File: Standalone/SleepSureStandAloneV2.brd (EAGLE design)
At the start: 62.3 x 37 mm, 66 parts, among them IC1 CP2104, Q1 mmbt2222, Q2 mmbt2222, Q3 DMG3415U, SW2 KMR2, U1 ADS1299-4PAG, U2 AP2112-3.3, U3 MCP73831T-2ACI/OT, X1 JSTPH, X2 ESP32_WROOM32_SKINNY, X4 20329

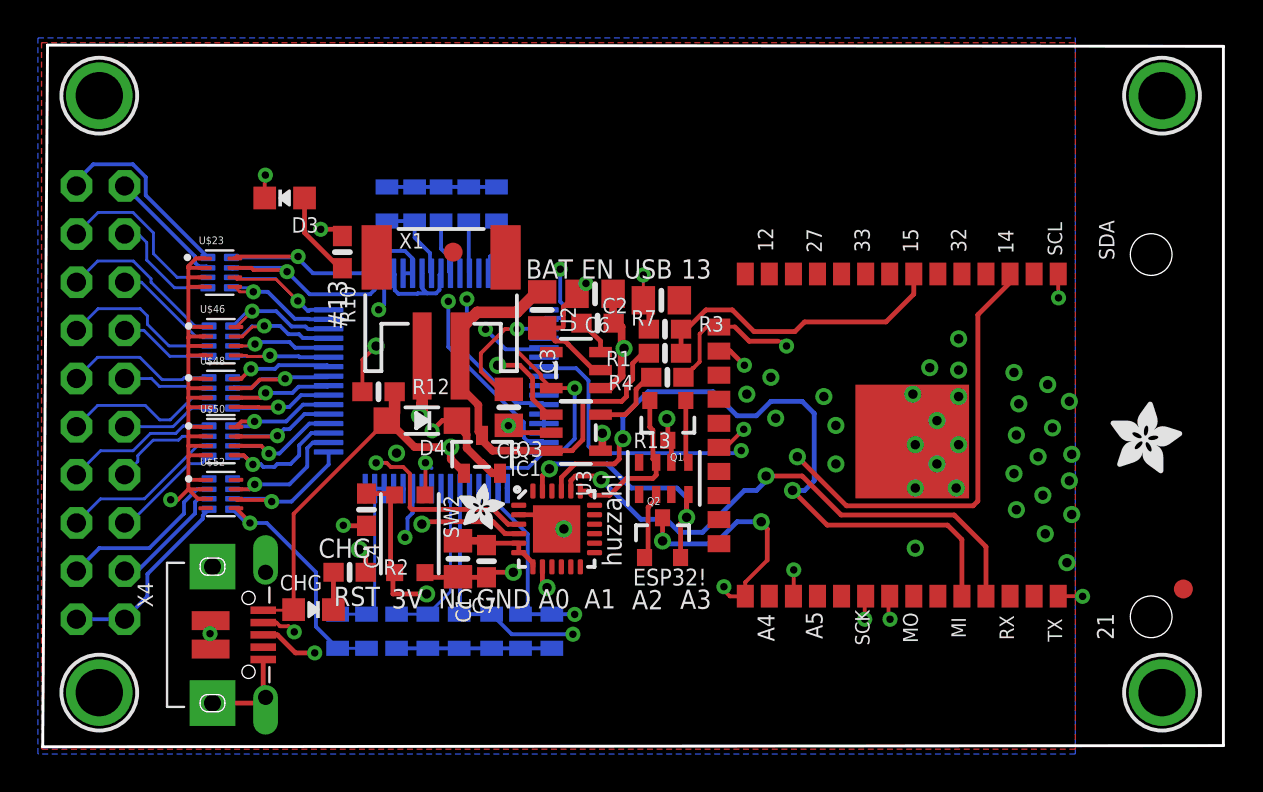
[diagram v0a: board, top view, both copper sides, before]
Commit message: modified design file and removed errors
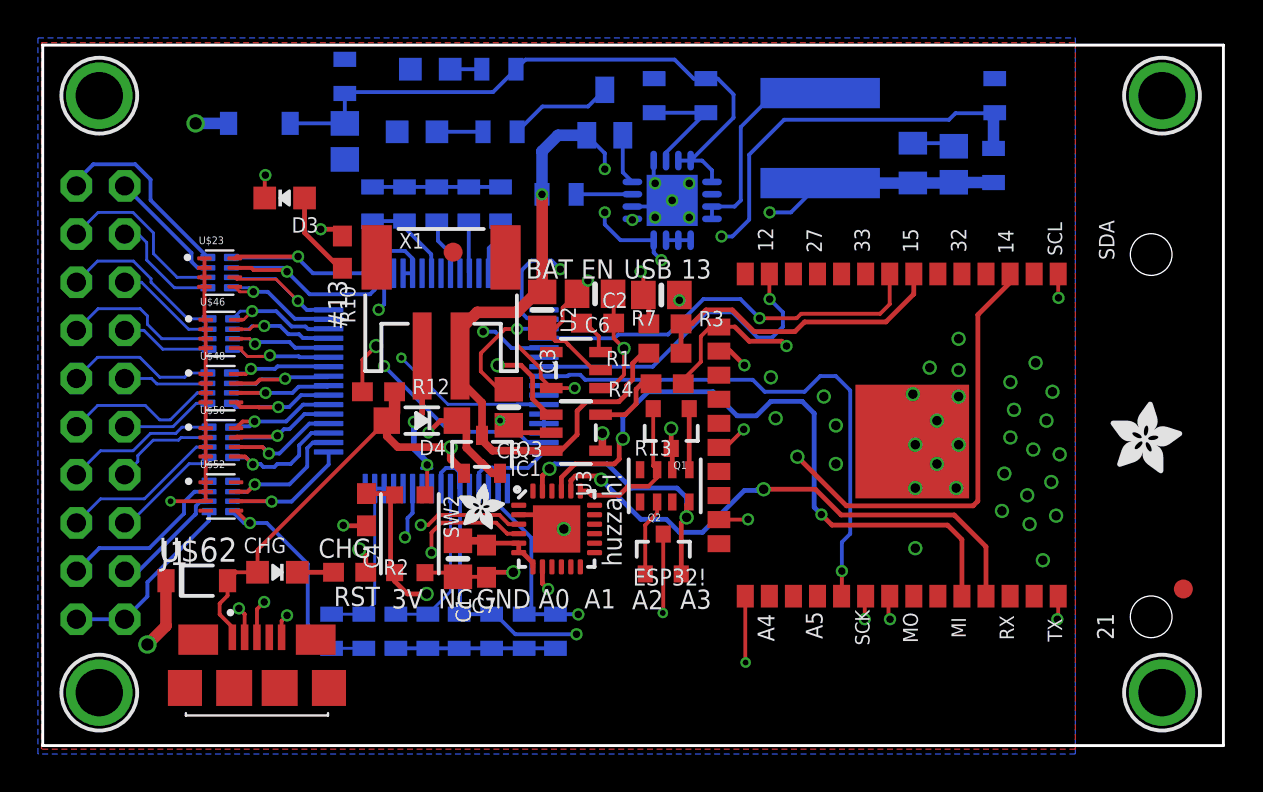
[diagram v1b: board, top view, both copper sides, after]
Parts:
- removed U$13: (no value), microbuilder:PCBFEAT-REV-040
- removed U$43: (no value), silks:HUZZAH32
- removed U$7: (no value), microbuilder:ADAFRUIT_5MM
- removed U$9: (no value), silks:FEATHERLOGO_MED
- removed X4: 20329, microbuilder:4UCONN_20329_V2
- added C17: 10uF, microbuilder:0805-NO
- added C18: 2.2uF, microbuilder:0805-NO
- added C19: 0.1uF, microbuilder:0805_10MGAP
- added C22: 100uF, SparkFun-Capacitors:0805
- added J1: 10118192-0002LF, ADS_Feather:AMPHENOL_10118192-0002LF
- added LED1: RED, microbuilder:CHIPLED_0805_NOOUTLINE
- added LED2: BLUE, microbuilder:CHIPLED_0805_NOOUTLINE
- added R11, R9: 1k, SparkFun-Resistors:0805
- added R16: 1.87M, SparkFun-Resistors:0805
- added R17: 340k, SparkFun-Resistors:0805
- added R18: 1.8M, SparkFun-Resistors:0805
- added R19, R5: 200k, SparkFun-Resistors:0805
- added T1: MMUN2133LT1G, transistor:SC59-BEC
- added U$55: 6.8uH, ADS_Feather:0628
- added U$62, U$66: MRB120, ADS_Feather:SOD123FL
- added U4: TPS61090RSAR, microbuilder:PVQFN-16
- U$23, U$46, U$48, U$50, U$52: value W2A45C103MAT2A -> 1nF
- U$44, U$45, U$47, U$49, U$51: value (none) -> 2.2k
- moved CHG 2.74 mm to (12.7, 9.14)
- moved Q2 0.86 mm to (33.1, 10.1)
- moved C13 0.76 mm to (17.7, 28.6)
- moved C10 0.53 mm to (19.4, 28.6)
- moved Q1 0.47 mm to (33.5, 16.8)
- moved R13 0.40 mm to (33.1, 13.7)
- moved U$45 0.38 mm to (9.72, 21.7)
- moved U$46 0.38 mm to (9.72, 21.7)
- moved R4 0.34 mm to (33.3, 19.1)
- moved C25 0.32 mm to (15.6, 6.03)
- moved C2 0.28 mm to (33.0, 23.8)
- moved R3 0.28 mm to (33.1, 22.3)
- moved U$47 0.26 mm to (9.65, 18.9)
- moved U$48 0.25 mm to (9.72, 18.9)
- moved C9 0.23 mm to (21.1, 28.6)
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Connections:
- removed net IO14_A6: X2.13
- removed net IO15_A8: X2.23
- removed net IO32_A7: X2.8
- removed net N$2: IC1.3, X4.D+
- removed net N$6: IC1.4, X4.D-
- removed net SCLK: U1.40
- new net 5VBAT: C18.1, C22.1, R18.2, R9.2, U$66.A, U4.1, U4.15, U4.16
- new net D+: IC1.3, J1.3
- new net D-: IC1.4, J1.2
- new net ENABLE: R5.1, U4.11
- new net GPIO0: Q2.3, X2.25
- new net IO16: X2.27
- new net LBO: T1.B, U4.12
- new net N$16: U$55.P$2, U4.3, U4.4
- new net N$17: R16.1, R17.2, U4.9
- new net N$18: R18.1, R19.2, U4.14
- new net N$19: LED2.A, R9.1
- new net N$20: LED1.A, R11.1
- new net N$21: R11.2, T1.C
- net 5V: now also U$62.C, U$66.C
- net ADS_CS: now also X2.13; no longer Q2.3, X2.25
- net ADS_RESET: now also X2.8
- net DRDY: now also X2.23; no longer X2.27
- net GND: now also C17.2, C18.2, C19.2, C22.2, J1.5, LED1.C, LED2.C, R17.1, R19.1, U4.10, U4.13, U4.5, U4.6, U4.7, U4.P$18, U4.P$19, U4.P$20, U4.P$21, U4.P$22, U4.THERMAL; no longer X4.BASE@1, X4.BASE@2, X4.GND, X4.SPRT@1, X4.SPRT@2, X4.SPRT@3, X4.SPRT@4
- net SCK: now also U1.40
- net VBAT: now also C17.1, C19.1, R16.2, R5.2, T1.E, U$55.P$1, U4.8
- net VBUS: now also J1.1, U$62.A; no longer X4.VBUS
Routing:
- net VBAT: track 25.0 -> 64.9 mm, vias 0 -> 5
- net 5VBAT: track 0.00 -> 33.5 mm
- net SCK: track 0.00 -> 28.3 mm, vias 0 -> 1
- net N$17: track 0.00 -> 26.1 mm, vias 0 -> 2
- net N$6: track 24.6 -> 0.00 mm, vias 3 -> 0
- net N$2: track 24.4 -> 0.00 mm, vias 2 -> 0
- net ADS_RESET: track 0.00 -> 21.4 mm, vias 0 -> 1
- net D-: track 0.00 -> 19.1 mm, vias 0 -> 2
- net D+: track 0.00 -> 18.0 mm, vias 0 -> 2
- net ADS_CS: track 35.5 -> 17.7 mm, vias 4 -> 1
- net GND: track 99.4 -> 85.7 mm
- net GPIO0: track 0.00 -> 13.1 mm, vias 0 -> 2
- net N$16: track 0.00 -> 11.1 mm
- net 5V: track 21.9 -> 30.4 mm, vias 3 -> 5
- net N$18: track 0.00 -> 6.13 mm
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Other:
- outline, holes or cut-outs redrawn
- board text removed: "12/A11"
- board text removed: "13/A12"
- board text removed: "14/A6"
- board text removed: "15/A8"
- board text removed: "27/A10"
- board text removed: "32/A7"
- board text removed: "33/A9"
- board text removed: "A0 DAC2"
- board text removed: "A1 DAC1"
- board text removed: "A2/34"
- board text removed: "A3/39"
- board text removed: "A4/36"
- board text removed: "A5/4"
- board text removed: "Contains FCCID 2AC7Z-ESP32"
- board text removed: "En"
- board text removed: "MISO/19"
- board text removed: "MOSI/18"
- board text removed: "RX/16"
- board text removed: "SCK/5"
- board text removed: "SCL/22"
- board text removed: "SDA/23"
- board text removed: "TX/17"
